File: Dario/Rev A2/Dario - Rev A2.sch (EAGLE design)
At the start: 31 parts, among them J1 1241050-5, J2 21_PIN, J3 21_PIN, SW1 KMR211G, U1 MK20DX256VLH7, Y1 8MHz, Y2 32.768kHz, 12.5pF

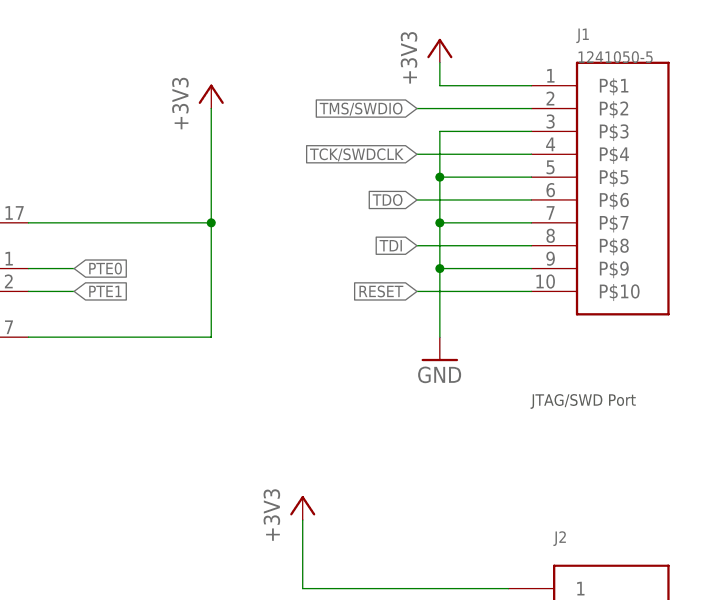
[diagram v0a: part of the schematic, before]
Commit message: Change the pin out of the jtag connector and change the width of all nets to 0.1778mm
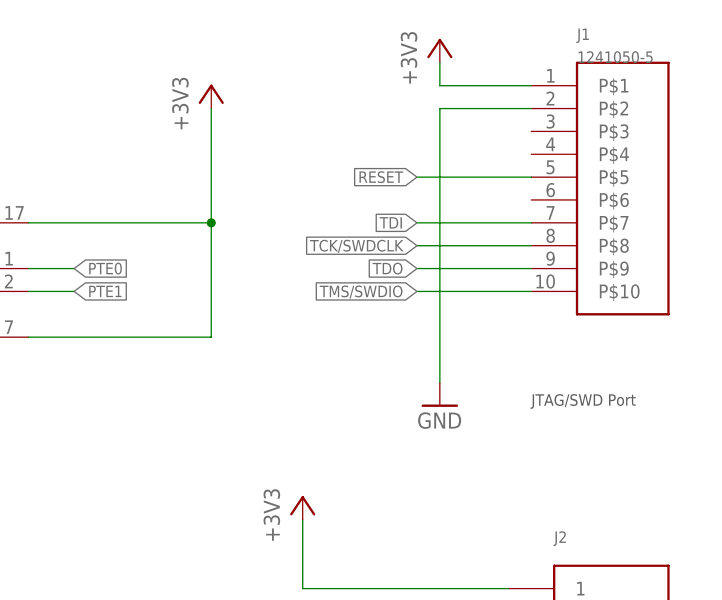
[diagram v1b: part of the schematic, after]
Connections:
- net GND: now also J1.P$2; no longer J1.P$3, J1.P$5, J1.P$7, J1.P$9
- net RESET: now also J1.P$5; no longer J1.P$10
- net TCK/SWDCLK: now also J1.P$8; no longer J1.P$4
- net TDI: now also J1.P$7; no longer J1.P$8
- net TDO: now also J1.P$9; no longer J1.P$6
- net TMS/SWDIO: now also J1.P$10; no longer J1.P$2
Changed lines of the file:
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@@
 <attribute name="MPN" x="33.02" y="243.84" size="1.778" layer="96" display="off"/>
 </instance>
-<instance part="GND7" gate="1" x="350.52" y="218.44"/>
+<instance part="GND7" gate="1" x="350.52" y="213.36"/>
 <instance part="+3V7" gate="G$1" x="350.52" y="254"/>
 <instance part="J2" gate="G$1" x="370.84" y="167.64">
@@
 <segment>
 <pinref part="GND7" gate="1" pin="GND"/>
-<wire x1="360.68" y1="243.84" x2="350.52" y2="243.84" width="0.1524" layer="91"/>
-<wire x1="350.52" y1="243.84" x2="350.52" y2="238.76" width="0.1524" layer="91"/>
-<wire x1="350.52" y1="238.76" x2="350.52" y2="233.68" width="0.1524" layer="91"/>
-<wire x1="350.52" y1="233.68" x2="350.52" y2="228.6" width="0.1524" layer="91"/>
-<wire x1="350.52" y1="228.6" x2="350.52" y2="220.98" width="0.1524" layer="91"/>
-<wire x1="360.68" y1="238.76" x2="350.52" y2="238.76" width="0.1524" layer="91"/>
-<junction x="350.52" y="238.76"/>
-<wire x1="360.68" y1="233.68" x2="350.52" y2="233.68" width="0.1524" layer="91"/>
-<junction x="350.52" y="233.68"/>
-<wire x1="360.68" y1="228.6" x2="350.52" y2="228.6" width="0.1524" layer="91"/>
-<junction x="350.52" y="228.6"/>
-<pinref part="J1" gate="G$1" pin="P$3"/>
-<pinref part="J1" gate="G$1" pin="P$5"/>
-<pinref part="J1" gate="G$1" pin="P$7"/>
-<pinref part="J1" gate="G$1" pin="P$9"/>
+<pinref part="J1" gate="G$1" pin="P$2"/>
+<wire x1="350.52" y1="215.9" x2="350.52" y2="246.38" width="0.1524" layer="91"/>
+<wire x1="350.52" y1="246.38" x2="360.68" y2="246.38" width="0.1524" layer="91"/>
 </segment>
 <segment>
@@
 <net name="TCK/SWDCLK" class="0">
 <segment>
-<wire x1="360.68" y1="241.3" x2="347.98" y2="241.3" width="0.1524" layer="91"/>
-<label x="347.98" y="241.3" size="1.27" layer="95" rot="R180" xref="yes"/>
-<pinref part="J1" gate="G$1" pin="P$4"/>
-</segment>
-<segment>
 <pinref part="U1" gate="A" pin="PTA0"/>
 <wire x1="137.16" y1="198.12" x2="124.46" y2="198.12" width="0.1524" layer="91"/>
 <label x="124.46" y="198.12" size="1.27" layer="95" rot="R180" xref="yes"/>
 </segment>
+<segment>
+<wire x1="360.68" y1="231.14" x2="347.98" y2="231.14" width="0.1524" layer="91"/>
+<label x="347.98" y="231.14" size="1.27" layer="95" rot="R180" xref="yes"/>
+<pinref part="J1" gate="G$1" pin="P$8"/>
+</segment>
 </net>
 <net name="TDO" class="0">
-<segment>
-<wire x1="360.68" y1="236.22" x2="347.98" y2="236.22" width="0.1524" layer="91"/>
-<label x="347.98" y="236.22" size="1.27" layer="95" rot="R180" xref="yes"/>
-<pinref part="J1" gate="G$1" pin="P$6"/>
-</segment>
 <segment>
 <pinref part="U1" gate="A" pin="PTA2"/>
@@
 <label x="124.46" y="193.04" size="1.27" layer="95" rot="R180" xref="yes"/>
 </segment>
+<segment>
+<wire x1="360.68" y1="228.6" x2="347.98" y2="228.6" width="0.1524" layer="91"/>
+<label x="347.98" y="228.6" size="1.27" layer="95" rot="R180" xref="yes"/>
+<pinref part="J1" gate="G$1" pin="P$9"/>
+</segment>
 </net>
 <net name="TDI" class="0">
-<segment>
-<wire x1="360.68" y1="231.14" x2="347.98" y2="231.14" width="0.1524" layer="91"/>
-<label x="347.98" y="231.14" size="1.27" layer="95" rot="R180" xref="yes"/>
-<pinref part="J1" gate="G$1" pin="P$8"/>
-</segment>
 <segment>
 <pinref part="U1" gate="A" pin="PTA1"/>
@@
 <label x="124.46" y="195.58" size="1.27" layer="95" rot="R180" xref="yes"/>
 </segment>
+<segment>
+<wire x1="360.68" y1="233.68" x2="347.98" y2="233.68" width="0.1524" layer="91"/>
+<label x="347.98" y="233.68" size="1.27" layer="95" rot="R180" xref="yes"/>
+<pinref part="J1" gate="G$1" pin="P$7"/>
+</segment>
 </net>
 <net name="TMS/SWDIO" class="0">
@@
 </segment>
 <segment>
-<wire x1="360.68" y1="246.38" x2="347.98" y2="246.38" width="0.1524" layer="91"/>
-<label x="347.98" y="246.38" size="1.27" layer="95" rot="R180" xref="yes"/>
-<pinref part="J1" gate="G$1" pin="P$2"/>
+<wire x1="360.68" y1="226.06" x2="347.98" y2="226.06" width="0.1524" layer="91"/>
+<label x="347.98" y="226.06" size="1.27" layer="95" rot="R180" xref="yes"/>
+<pinref part="J1" gate="G$1" pin="P$10"/>
 </segment>
 </net>
@@
 </segment>
 <segment>
-<wire x1="360.68" y1="226.06" x2="347.98" y2="226.06" width="0.1524" layer="91"/>
-<label x="347.98" y="226.06" size="1.27" layer="95" rot="R180" xref="yes"/>
-<pinref part="J1" gate="G$1" pin="P$10"/>
-</segment>
-<segment>
 <pinref part="U1" gate="A" pin="PTA5"/>
 <wire x1="137.16" y1="185.42" x2="124.46" y2="185.42" width="0.1524" layer="91"/>
 <label x="124.46" y="185.42" size="1.27" layer="95" rot="R180" xref="yes"/>
 </segment>
-</net>
+<segment>
+<wire x1="360.68" y1="238.76" x2="347.98" y2="238.76" width="0.1524" layer="91"/>
+<label x="347.98" y="238.76" size="1.27" layer="95" rot="R180" xref="yes"/>
+<pinref part="J1" gate="G$1" pin="P$5"/>
+</segment>
+</net>
